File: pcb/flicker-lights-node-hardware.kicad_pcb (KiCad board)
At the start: 2 copper layers, 59.7 x 48.3 mm, 31 parts, among them IC1 ATMEGA168PA-MM, P1 CONN_01X06, P2 CONN_01X02, P3 CONN_02X04, P4 CONN_02X03, P5 CONN_01X04, P6 CONN_01X04, Q1 BSS138, Q2 BSS138, Q3 BSS138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

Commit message: First layout attempt done, new board outline with better dimensioning. Added a preview picture.
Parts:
- removed the REF** at (193.7, 118.1)
- removed the REF** at (221.6, 119.1)
- removed the REF** at (193.7, 146.2)
- removed the REF** at (221.6, 146.2)
- added REF**: MountingHole_3.2mm_M3_ISO14580_Pad, Mounting_Holes:MountingHole_3.2mm_M3_ISO14580_Pad, F.Cu at (77.0, 197.3)
- added REF**: MountingHole_3.2mm_M3_ISO14580_Pad, Mounting_Holes:MountingHole_3.2mm_M3_ISO14580_Pad, F.Cu at (49.0, 197.3)
- added REF**: MountingHole_3.2mm_M3_ISO14580_Pad, Mounting_Holes:MountingHole_3.2mm_M3_ISO14580_Pad, F.Cu at (77.0, 169.3)
- added REF**: MountingHole_3.2mm_M3_ISO14580_Pad, Mounting_Holes:MountingHole_3.2mm_M3_ISO14580_Pad, F.Cu at (49.0, 169.3)
- IC1: value ATMEGA168PA-MM -> ATMEGA168PA-A; footprint Housings_DFN_QFN:QFN-28-1EP_4x4mm_Pitch0.4mm -> Housings_QFP:LQFP-32_7x7mm_Pitch0.8mm
- moved R1 248.3 mm to (51.5, 181.0), turned to 270 degrees
- moved R2 243.0 mm to (51.5, 184.5), turned to 270 degrees
- moved R4 242.9 mm to (45.0, 162.7)
- moved D1 242.5 mm to (45.0, 159.7)
- moved Q3 241.8 mm to (55.0, 175.7)
- moved Q2 229.4 mm to (62.0, 171.2)
- moved C6 224.2 mm to (61.2, 168.2)
- moved Q1 224.1 mm to (57.5, 171.2)
- moved R3 216.9 mm to (73.8, 182.7), turned to 180 degrees
- moved C3 216.2 mm to (64.8, 189.2)
- moved Q6 216.0 mm to (66.5, 171.2)
- moved C7 215.4 mm to (72.0, 167.7)
- moved U2 204.2 mm to (40.0, 183.0), turned to 90 degrees
- moved C1 197.8 mm to (69.5, 205.7)
- moved Q5 193.9 mm to (74.0, 175.2)
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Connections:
- IC1 pad 10: Net-(IC1-Pad10) -> /LED_GREEN
- IC1 pad 11: /NRF24_CE -> Net-(D1-Pad2)
- IC1 pad 12: /NRF24_CSN -> Net-(IC1-Pad12)
- IC1 pad 13: /NRF24_MO -> /NRF24_CE
- IC1 pad 14: /NRF24_MI -> /NRF24_CSN
- IC1 pad 15: /NRF24_SCK -> /NRF24_MO
- IC1 pad 16: +3V3 -> /NRF24_MI
- IC1 pad 17: Net-(C3-Pad1) -> /NRF24_SCK
- IC1 pad 18: GND -> +3V3
- IC1 pad 19: /ADC_9V -> Net-(IC1-Pad19)
- IC1 pad 20: Net-(D1-Pad2) -> Net-(C3-Pad1)
- IC1 pad 21: Net-(IC1-Pad21) -> GND
- IC1 pad 23: Net-(IC1-Pad23) -> /VADC
- IC1 pad 26: /FTDI_RX -> Net-(IC1-Pad26)
- IC1 pad 27: /FTDI_TX -> Net-(IC1-Pad27)
- IC1 pad 29: (no net) -> Net-(IC1-Pad29)
- IC1 pad 3: +3V3 -> GND
- IC1 pad 4: GND -> +3V3
- IC1 pad 5: Net-(IC1-Pad5) -> GND
- IC1 pad 6: Net-(IC1-Pad6) -> +3V3
- IC1 pad 7: /LED_RED -> Net-(IC1-Pad7)
- IC1 pad 8: /LED_GREEN -> Net-(IC1-Pad8)
- IC1 pad 9: Net-(IC1-Pad9) -> /LED_RED
- P4 pad 5: Net-(IC1-Pad25) -> Net-(IC1-Pad29)
- R1 pad 2: /ADC_9V -> /VADC
- R2 pad 1: /ADC_9V -> /VADC
- R3 pad 2: Net-(IC1-Pad25) -> Net-(IC1-Pad29)
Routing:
- net +3V3: track 0.00 -> 115.2 mm, vias 0 -> 4
- net +9V: track 0.00 -> 66.1 mm
- net /NRF24_MO: track 0.00 -> 53.7 mm, vias 0 -> 2
- net GND: track 0.00 -> 39.1 mm, vias 0 -> 16
- net Net-(D1-Pad2): track 0.00 -> 38.0 mm, vias 0 -> 2
- net /NRF24_SCK: track 0.00 -> 37.6 mm, vias 0 -> 1
- net /NRF24_CE: track 0.00 -> 35.8 mm
- net /NRF24_MI: track 0.00 -> 33.5 mm, vias 0 -> 2
- net Net-(IC1-Pad29): track 0.00 -> 29.2 mm, vias 0 -> 2
- net /LED_GREEN: track 0.00 -> 28.5 mm, vias 0 -> 3
- net /VADC: track 0.00 -> 25.6 mm, vias 0 -> 2
- net /NRF24_CSN: track 0.00 -> 24.6 mm, vias 0 -> 1
- net /LED_RED: track 0.00 -> 22.7 mm, vias 0 -> 3
- net /FTDI_TX: track 0.00 -> 22.6 mm
- net /FTDI_RX: track 0.00 -> 21.9 mm
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- added copper zone on B.Cu, net (none)
- added copper zone on B.Cu, net GND
- added copper zone on F.Cu, net GND
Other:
- board size 59.7 x 48.3 mm -> 59.7 x 48.9 mm

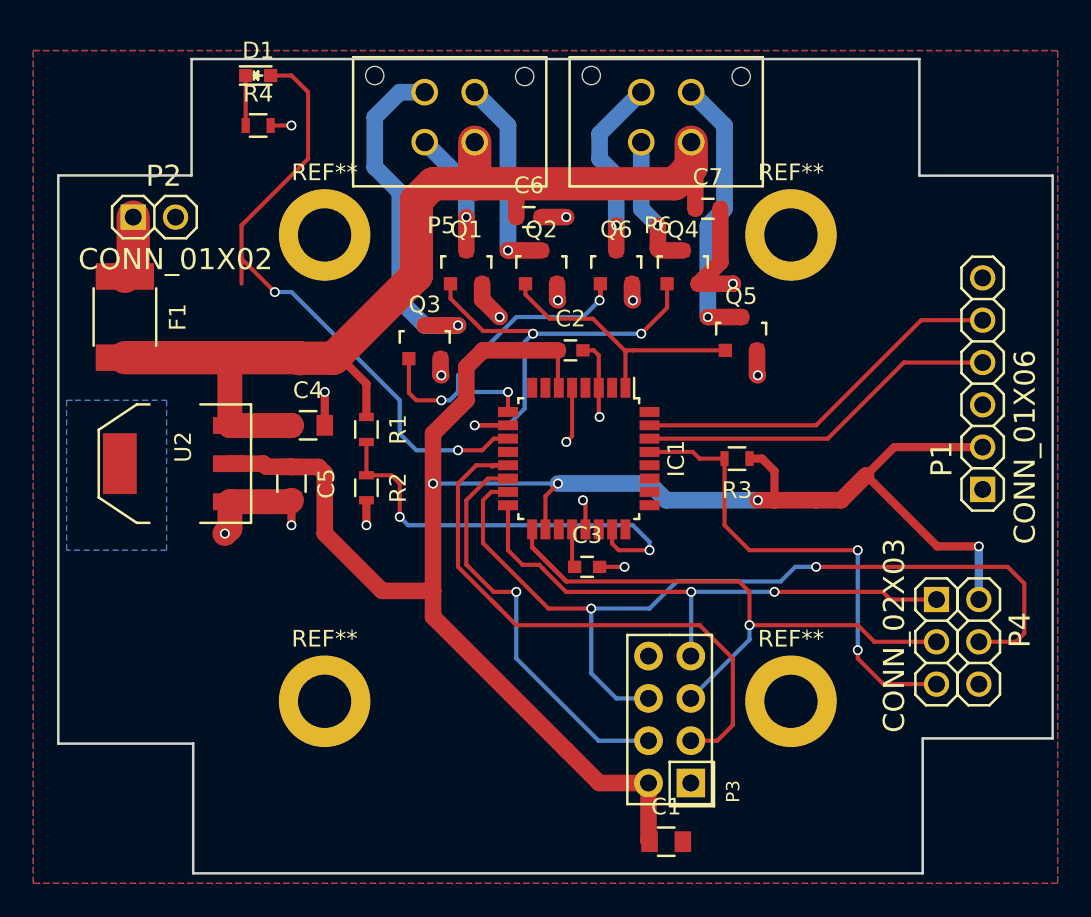
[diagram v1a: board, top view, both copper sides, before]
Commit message: Finished cleaning up silkscreen
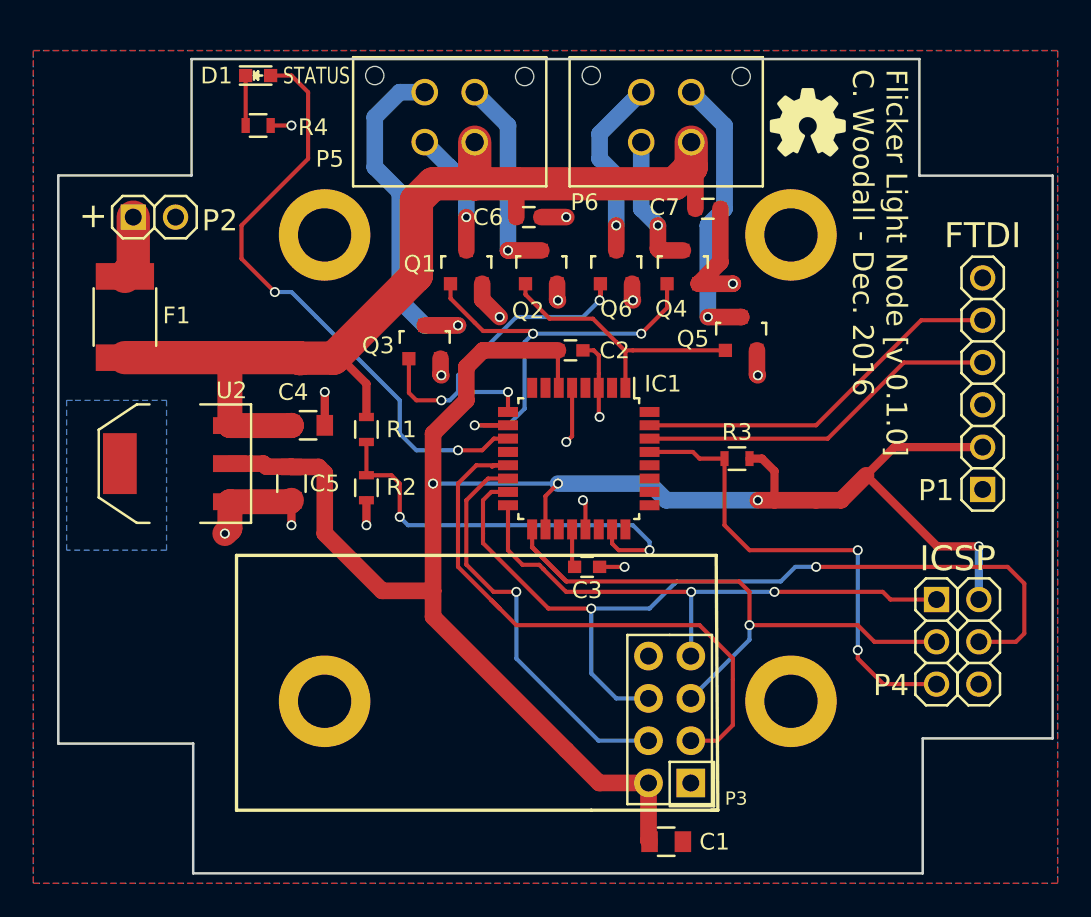
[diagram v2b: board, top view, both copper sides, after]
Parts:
- added ?: , xess:oshw-logo2, F.Cu at (78.0, 162.6)
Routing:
- net Net-(D1-Pad2): track 38.0 -> 36.5 mm
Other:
- board text added: "+"
- board text added: "FTDI"
- board text added: "Flicker Light Node [v 0.1.0] C. Woodall - Dec. 2016"
- board text added: "ICSP"
- board text added: "STATUS"

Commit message: Added script for generating BOM (from https://productize.be/kicad-bom-generation/), and added BOM
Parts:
- moved ? 50.2 mm to (38.5, 193.4)
- moved C3 6.73 mm to (70.9, 186.5), turned to 90 degrees
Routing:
- net +3V3: track 115.2 -> 126.3 mm
- net Net-(C3-Pad1): track 2.31 -> 10.6 mm
- net GND: track 39.1 -> 40.7 mm, vias 16 -> 18

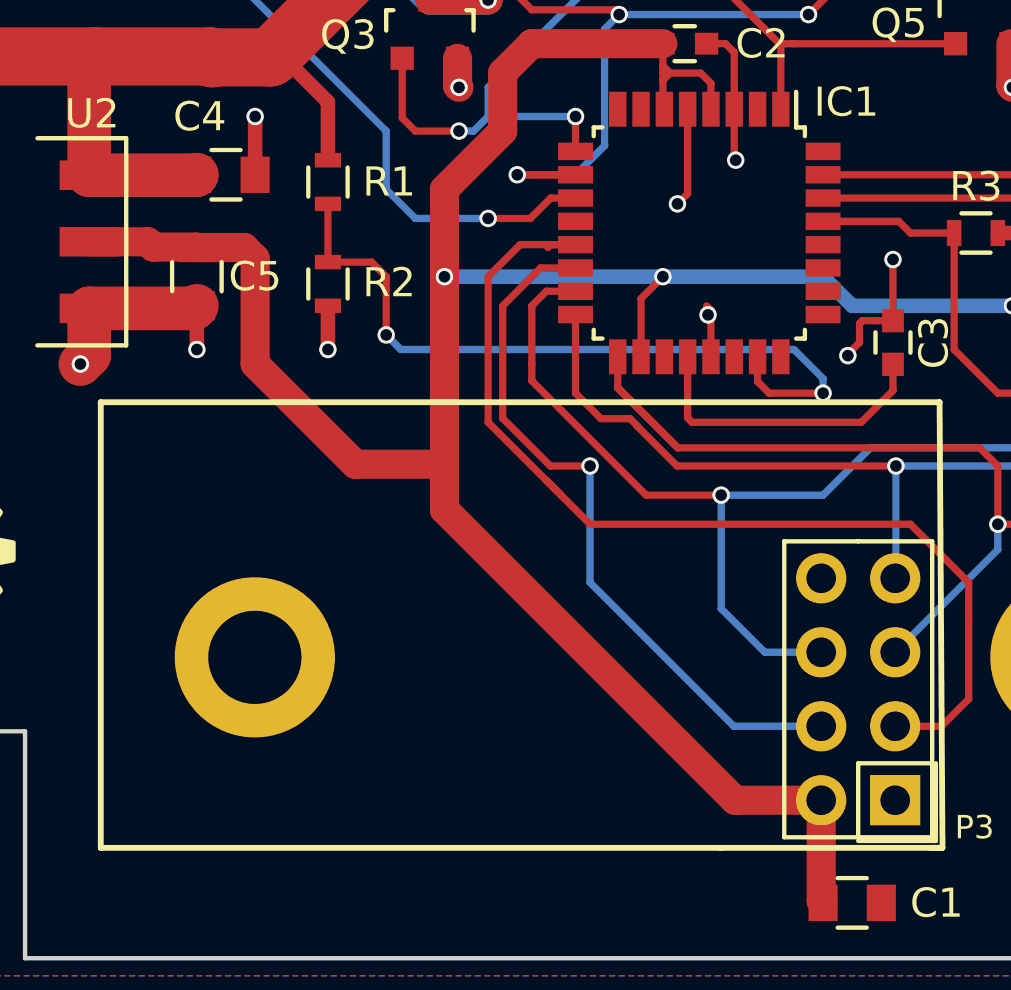
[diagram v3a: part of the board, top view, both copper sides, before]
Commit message: Removed copper from underneath radio module
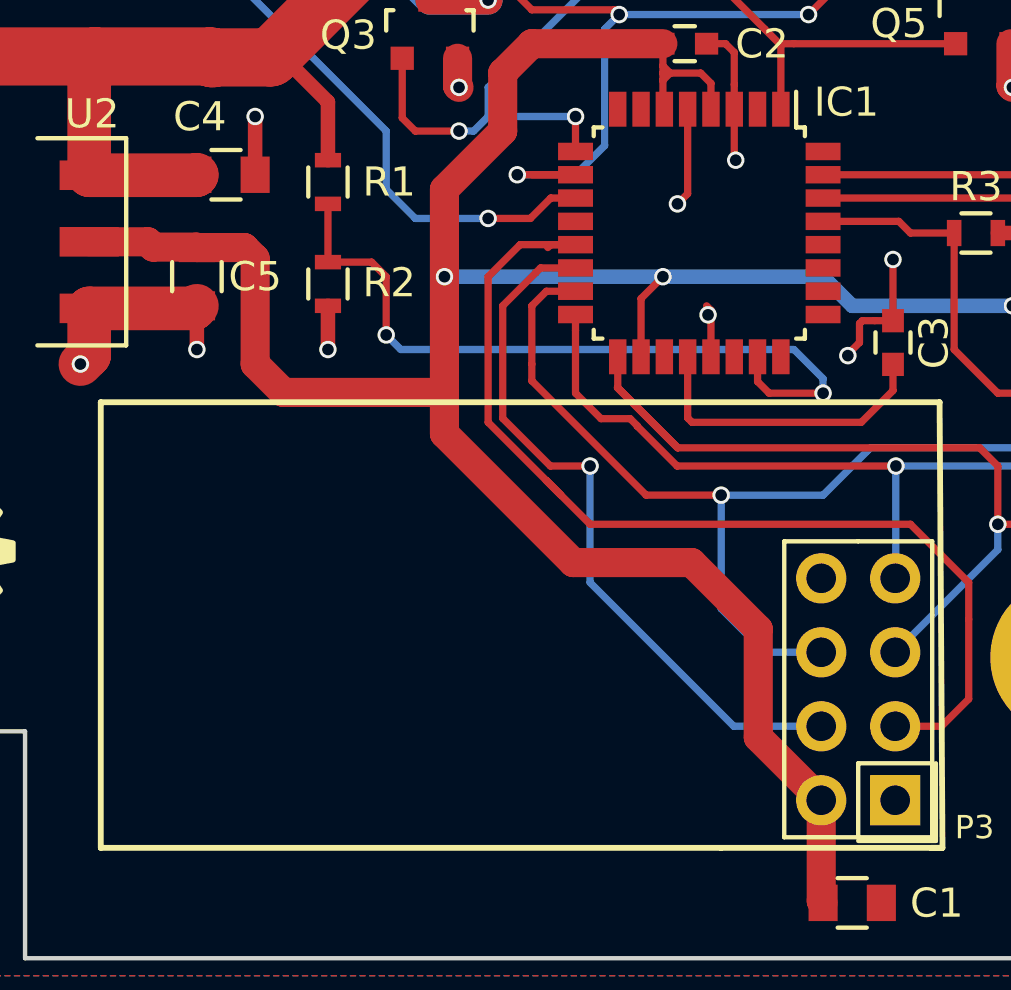
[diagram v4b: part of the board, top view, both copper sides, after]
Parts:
- removed the REF** at (49.0, 197.3)
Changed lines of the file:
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@@
     (thickness 1.6)
     (drawings 49)
-    (tracks 378)
+    (tracks 380)
     (zones 0)
-    (modules 32)
+    (modules 31)
     (nets 41)
   )
@@
     (38 B.Mask user)
     (39 F.Mask user)
-    (40 Dwgs.User user hide)
+    (40 Dwgs.User user)
     (41 Cmts.User user)
     (42 Eco1.User user)
@@
     (trace_clearance 0.2)
     (zone_clearance 0.508)
-    (zone_45_only no)
+    (zone_45_only yes)
     (trace_min 0.2)
     (segment_width 0.2)
@@
     (visible_elements FFFFFF7F)
     (pcbplotparams
-      (layerselection 0x00030_80000001)
+      (layerselection 0x010f0_80000001)
       (usegerberextensions false)
-      (excludeedgelayer true)
+      (excludeedgelayer false)
       (linewidth 0.100000)
       (plotframeref false)
@@
       (plotinvisibletext false)
       (padsonsilk false)
-      (subtractmaskfromsilk false)
+      (subtractmaskfromsilk true)
       (outputformat 1)
       (mirror false)
-      (drillshape 1)
+      (drillshape 0)
       (scaleselection 1)
-      (outputdirectory ""))
+      (outputdirectory output/))
   )
   (net 0 "")
@@
   (module Mounting_Holes:MountingHole_3.2mm_M3_ISO14580_Pad (layer F.Cu)
     (at 76.99 197.31)
-    (descr "Mounting Hole 3.2mm, M3, ISO14580")
-    (tags "mounting hole 3.2mm m3 iso14580")
-    (fp_text reference REF** (at 0 -3.75) (layer F.SilkS) hide
-      (effects (font (size 1 1) (thickness 0.15)))
-    )
-    (fp_text value MountingHole_3.2mm_M3_ISO14580_Pad (at 0 3.75) (layer F.Fab)
-      (effects (font (size 1 1) (thickness 0.15)))
-    )
-    (fp_circle (center 0 0) (end 2.75 0) (layer Cmts.User) (width 0.15))
-    (fp_circle (center 0 0) (end 3 0) (layer F.CrtYd) (width 0.05))
-    (pad 1 thru_hole circle (at 0 0) (size 5.5 5.5) (drill 3.2) (layers *.Cu *.Mask F.SilkS))
-  )
-  (module Mounting_Holes:MountingHole_3.2mm_M3_ISO14580_Pad (layer F.Cu)
-    (at 48.99 197.31)
     (descr "Mounting Hole 3.2mm, M3, ISO14580")
     (tags "mounting hole 3.2mm m3 iso14580")
@@
   )
   (gr_line (start 33 158.75) (end 92.73 158.75) (angle 90) (layer Dwgs.User) (width 0.2))
+  (segment (start 55.5 188.214) (end 55.5 189.632) (width 1) (layer F.Cu) (net 1))
+  (segment (start 55.5 189.632) (end 59.924 194.056) (width 1) (layer F.Cu) (net 1))
+  (segment (start 63.988 194.056) (end 66.274 196.342) (width 1) (layer F.Cu) (net 1))
+  (segment (start 59.924 194.056) (end 63.988 194.056) (width 1) (layer F.Cu) (net 1))
+  (segment (start 66.274 196.342) (end 66.274 200.054) (width 1) (layer F.Cu) (net 1))
+  (segment (start 66.274 200.054) (end 68.436 202.216) (width 1) (layer F.Cu) (net 1))
+  (segment (start 55.5 181.24) (end 55.5 188.214) (width 1) (layer F.Cu) (net 1))
+  (segment (start 55.5 188.214) (end 49.974 188.214) (width 1) (layer F.Cu) (net 1))
+  (segment (start 49.974 188.214) (end 49 187.24) (width 1) (layer F.Cu) (net 1))
   (segment (start 76.9 185.24) (end 76.65 185.24) (width 0.5) (layer F.Cu) (net 1))
   (segment (start 78.5 185.24) (end 76.9 185.24) (width 0.5) (layer F.Cu) (net 1))
@@
   (segment (start 62.25 184.99) (end 63 184.24) (width 0.25) (layer F.Cu) (net 1))
   (via (at 63 184.24) (size 0.6) (drill 0.4) (layers F.Cu B.Cu) (net 1))
-  (segment (start 55.5 190.680001) (end 55.5 192.24) (width 1) (layer F.Cu) (net 1))
-  (segment (start 55.5 192.24) (end 63.5 200.24) (width 1) (layer F.Cu) (net 1))
-  (segment (start 52.440001 190.680001) (end 55.5 190.680001) (width 1) (layer F.Cu) (net 1))
   (segment (start 63 176.24) (end 58.5 176.24) (width 1) (layer F.Cu) (net 1))
   (segment (start 58.5 176.24) (end 57.5 177.24) (width 1) (layer F.Cu) (net 1))
   (segment (start 57.5 177.24) (end 57.5 179.24) (width 1) (layer F.Cu) (net 1))
   (segment (start 57.5 179.24) (end 55.5 181.24) (width 1) (layer F.Cu) (net 1))
-  (segment (start 55.5 181.24) (end 55.5 190.680001) (width 1) (layer F.Cu) (net 1))
   (segment (start 63 178.44) (end 63.05 178.49) (width 0.25) (layer F.Cu) (net 1))
   (segment (start 68.436 202.216) (end 68.436 205.676) (width 1) (layer F.Cu) (net 1))
@@
   (segment (start 48.625 183.24) (end 49 183.615) (width 1) (layer F.Cu) (net 1))
   (segment (start 49 183.615) (end 49 187.24) (width 1) (layer F.Cu) (net 1))
-  (segment (start 49 187.24) (end 52.440001 190.680001) (width 1) (layer F.Cu) (net 1))
-  (segment (start 63.5 200.24) (end 65.476 202.216) (width 1) (layer F.Cu) (net 1))
-  (segment (start 65.476 202.216) (end 68.436 202.216) (width 1) (layer F.Cu) (net 1))
   (segment (start 45.5 183.224) (end 46.984 183.224) (width 1) (layer F.Cu) (net 1))
   (segment (start 46.984 183.224) (end 47 183.24) (width 1) (layer F.Cu) (net 1))
@@
       )
     )
+  )
+  (zone (net 0) (net_name "") (layer B.Cu) (hatch edge 0.508)
+    (connect_pads (clearance 0.508))
+    (min_thickness 0.254)
+    (keepout (tracks allowed) (vias allowed) (copperpour not_allowed))
+    (fill yes (arc_segments 16) (thermal_gap 0.508) (thermal_bridge_width 0.508))
+    (polygon
+      (pts
+        (xy 48.494 188.468) (xy 55.013933 188.468) (xy 55.013933 211.836) (xy 32.972106 211.836) (xy 32.718106 188.468)
+        (xy 42.652 188.468) (xy 43.668 187.452) (xy 47.478 187.452)
+      )
+    )
+  )
+  (zone (net 0) (net_name "") (layer F.Cu) (hatch edge 0.508)
+    (connect_pads (clearance 0.508))
+    (min_thickness 0.254)
+    (keepout (tracks allowed) (vias allowed) (copperpour not_allowed))
+    (fill yes (arc_segments 16) (thermal_gap 0.508) (thermal_bridge_width 0.508))
+    (polygon
+      (pts
+        (xy 48.494 188.468) (xy 54.816106 188.468) (xy 54.816106 211.836) (xy 32.972106 211.836) (xy 32.718106 188.468)
+        (xy 42.652 188.468) (xy 43.668 187.452) (xy 47.478 187.452)
+      )
+    )
